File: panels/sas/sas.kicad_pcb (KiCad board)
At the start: 2 copper layers, 140 x 140 mm, 10 parts

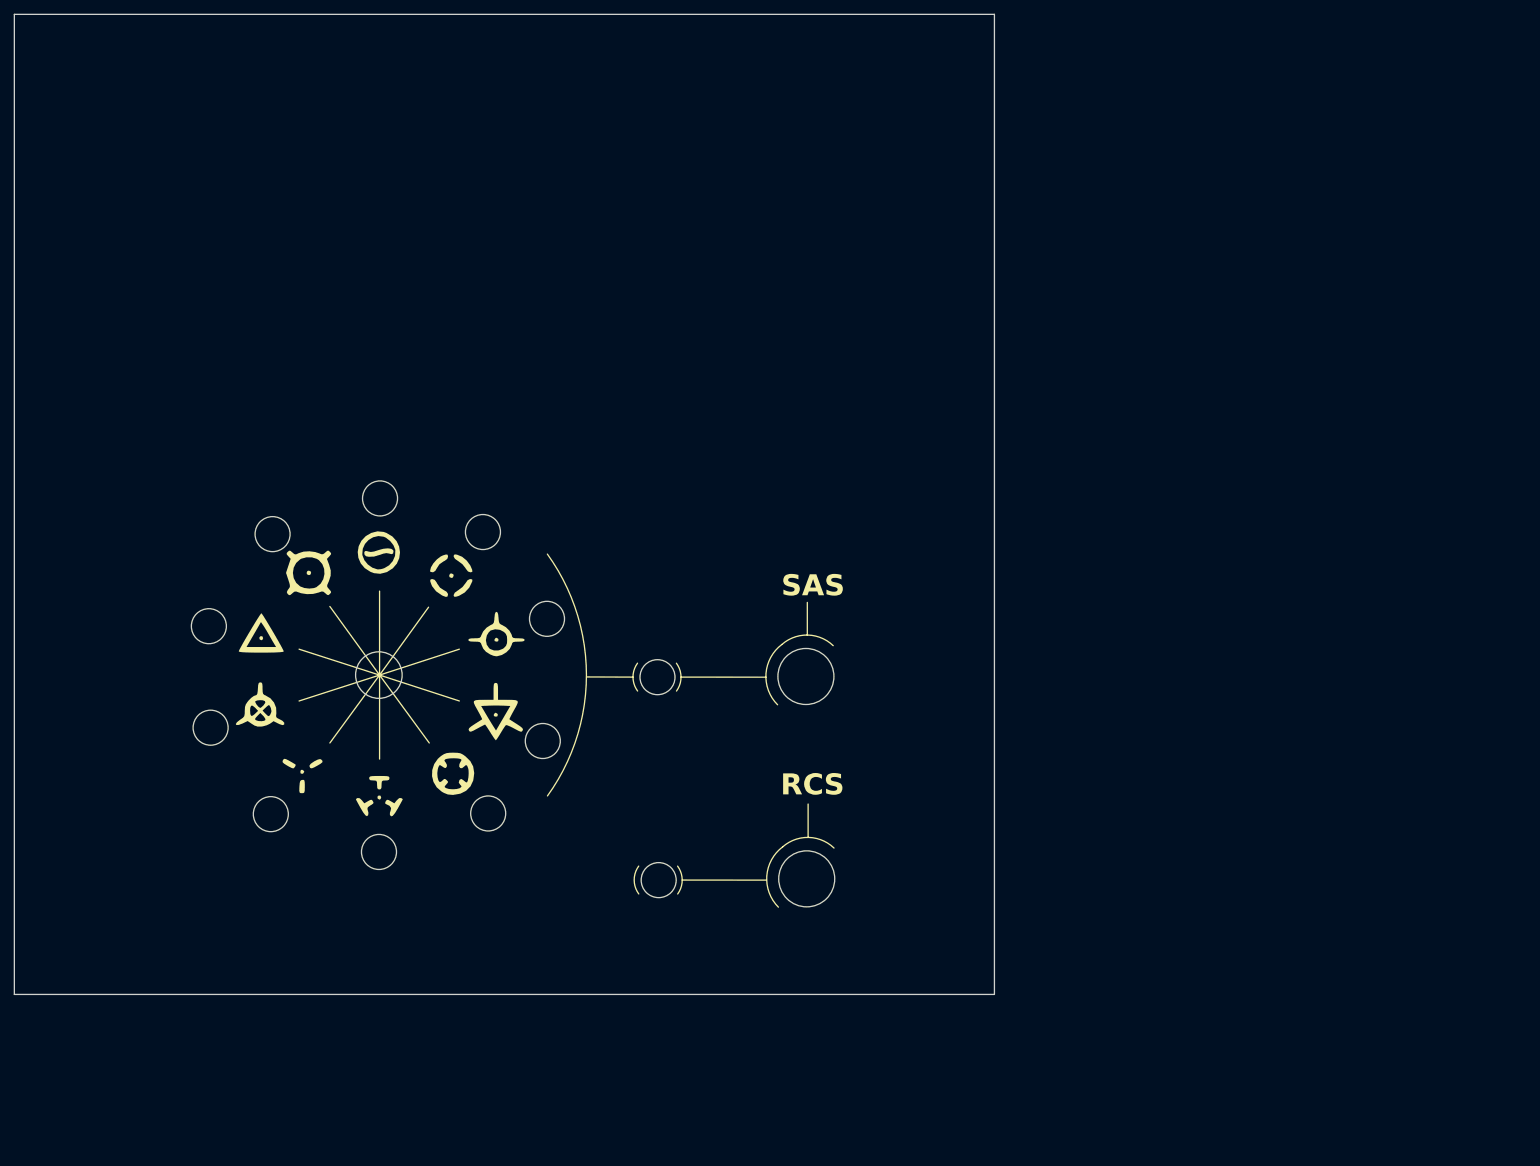
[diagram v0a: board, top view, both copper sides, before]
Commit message: Panels: rework of ctrl and sas. Add gauges and v1 of executive
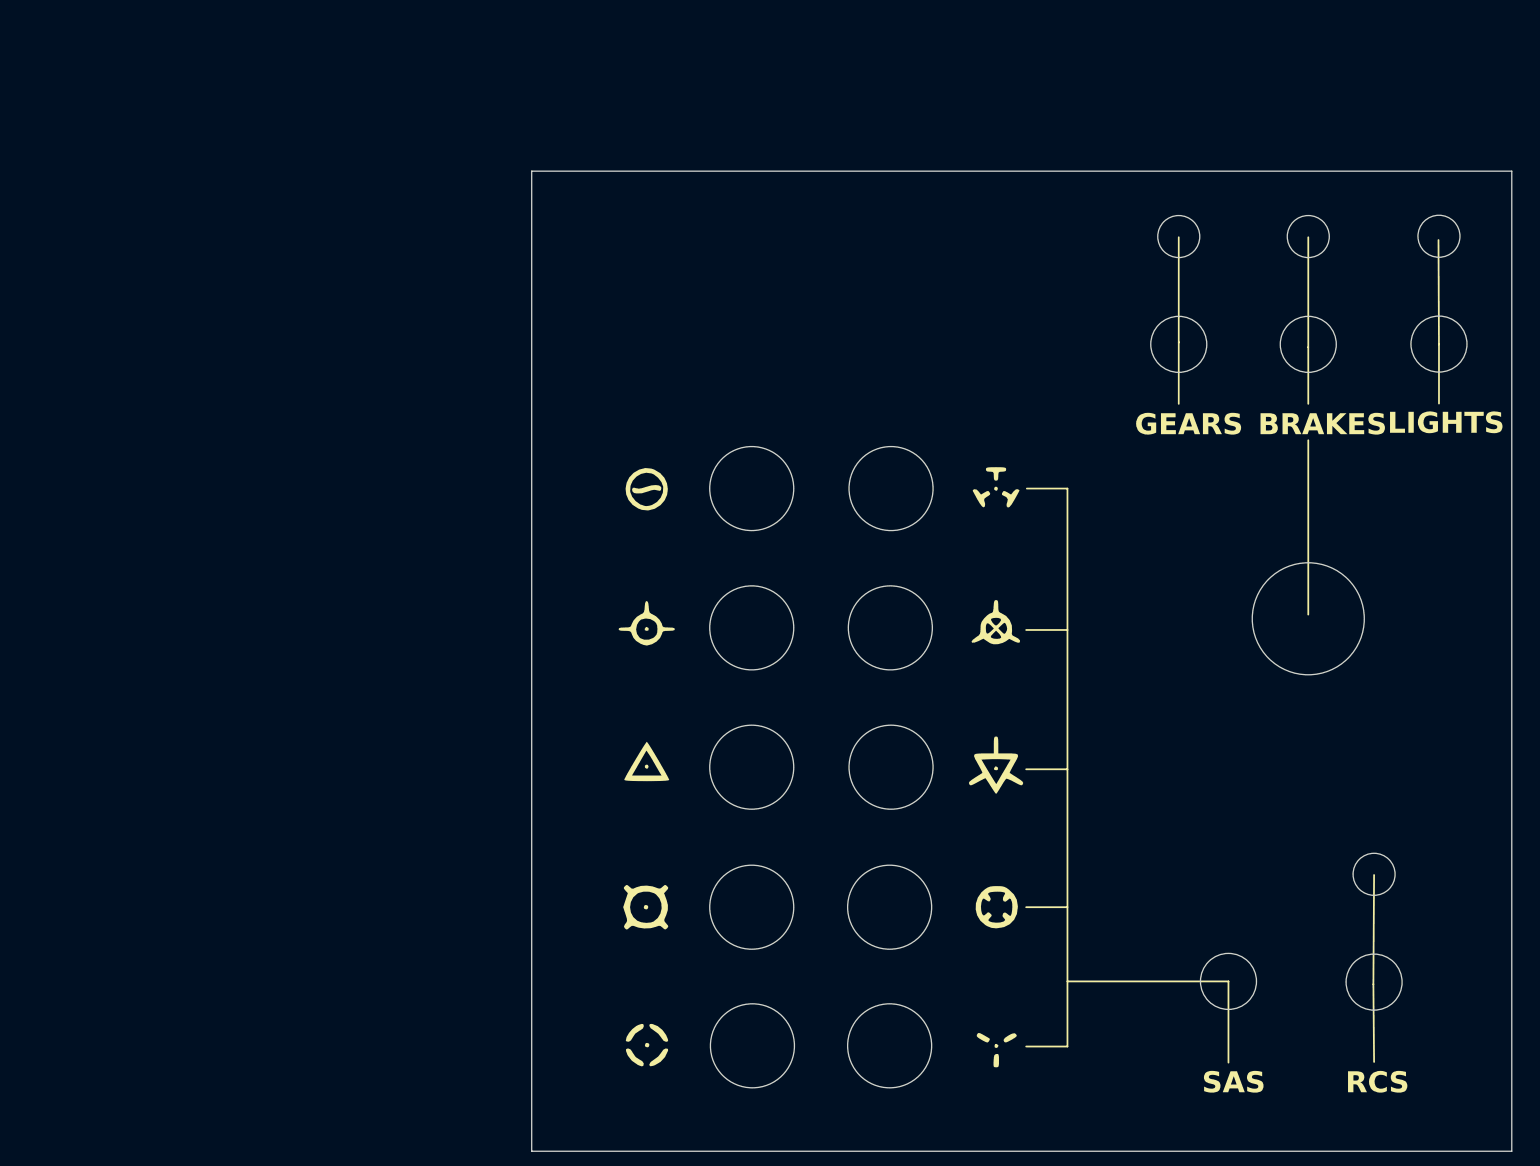
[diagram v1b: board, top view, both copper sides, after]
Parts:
- moved G*** 106.6 mm to (140.3, 147.8)
- moved G*** 105.8 mm to (140.2, 86.8)
- moved G*** 98.5 mm to (140.2, 67.7)
- moved G*** 80.0 mm to (140.3, 127.5)
- moved G*** 72.7 mm to (90.2, 147.2)
- moved G*** 71.9 mm to (140.2, 107.3)
- moved G*** 67.8 mm to (90.2, 127.5)
- moved G*** 58.0 mm to (90.3, 106.6)
- moved G*** 39.3 mm to (90.3, 67.8)
- moved G*** 21.5 mm to (90.3, 86.9)
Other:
- outline, holes or cut-outs redrawn
- board text added: "BRAKES"
- board text added: "GEARS"
- board text added: "LIGHTS"
- board text removed: "C111418"
- board text removed: "C264310"
- board text removed: "C2764902"
- board text removed: "C2764903"
- board text removed: "C330764"
- board text removed: "C779441"
- board text removed: "C841514"
- board text removed: "C99697"
- board text removed: "MA00L1NZQD F10611-ND"
